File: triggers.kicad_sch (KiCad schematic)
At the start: 37 parts, among them U10 SN74LVC2G17DC, U13 SRV05-4, U14 SN74LVC2G17DC, U15 SRV05-4, U28 74HC14, U9 SN74LVC2G17DC

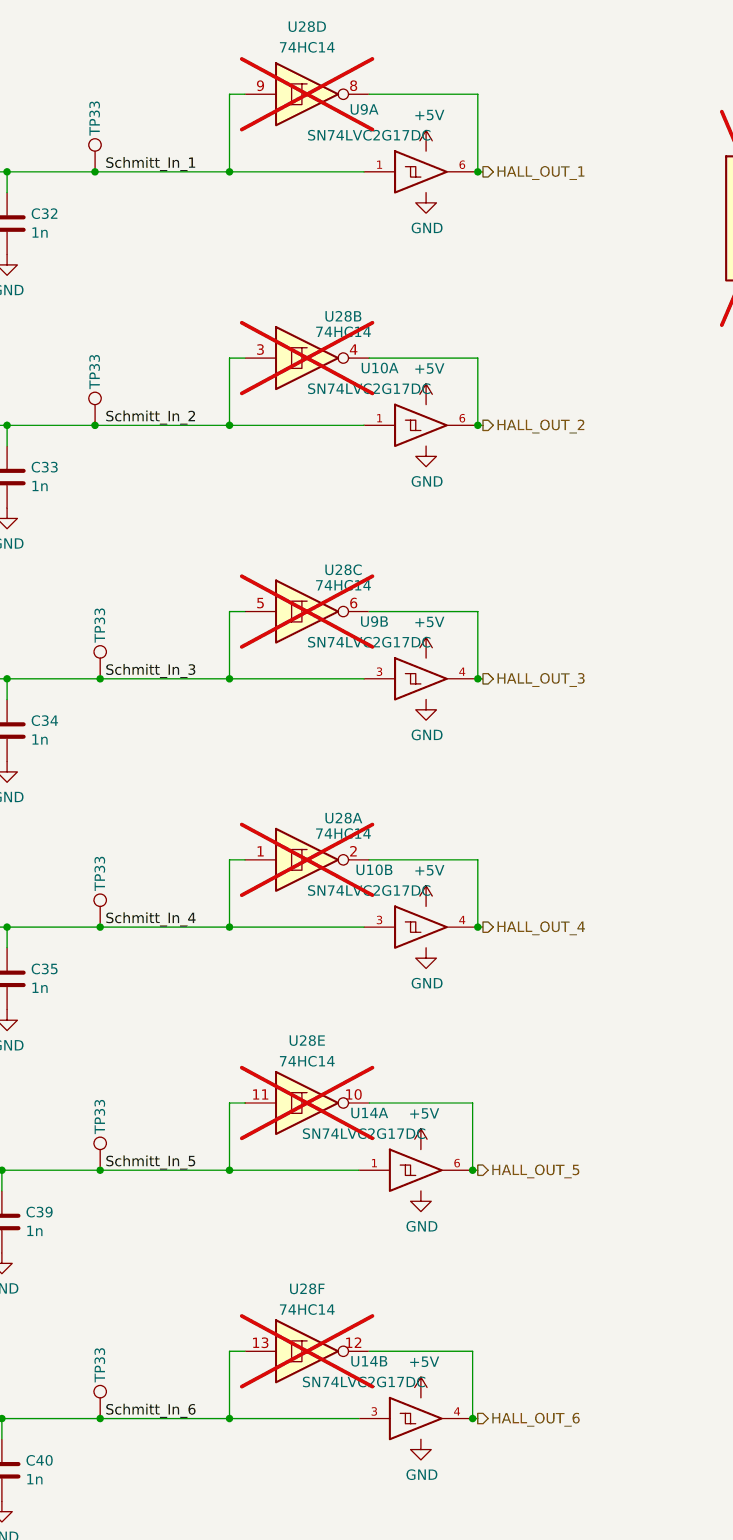
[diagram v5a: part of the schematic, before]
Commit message: Change U9,U10,U14 to SN74LVC2G17DBVR, version as ordered
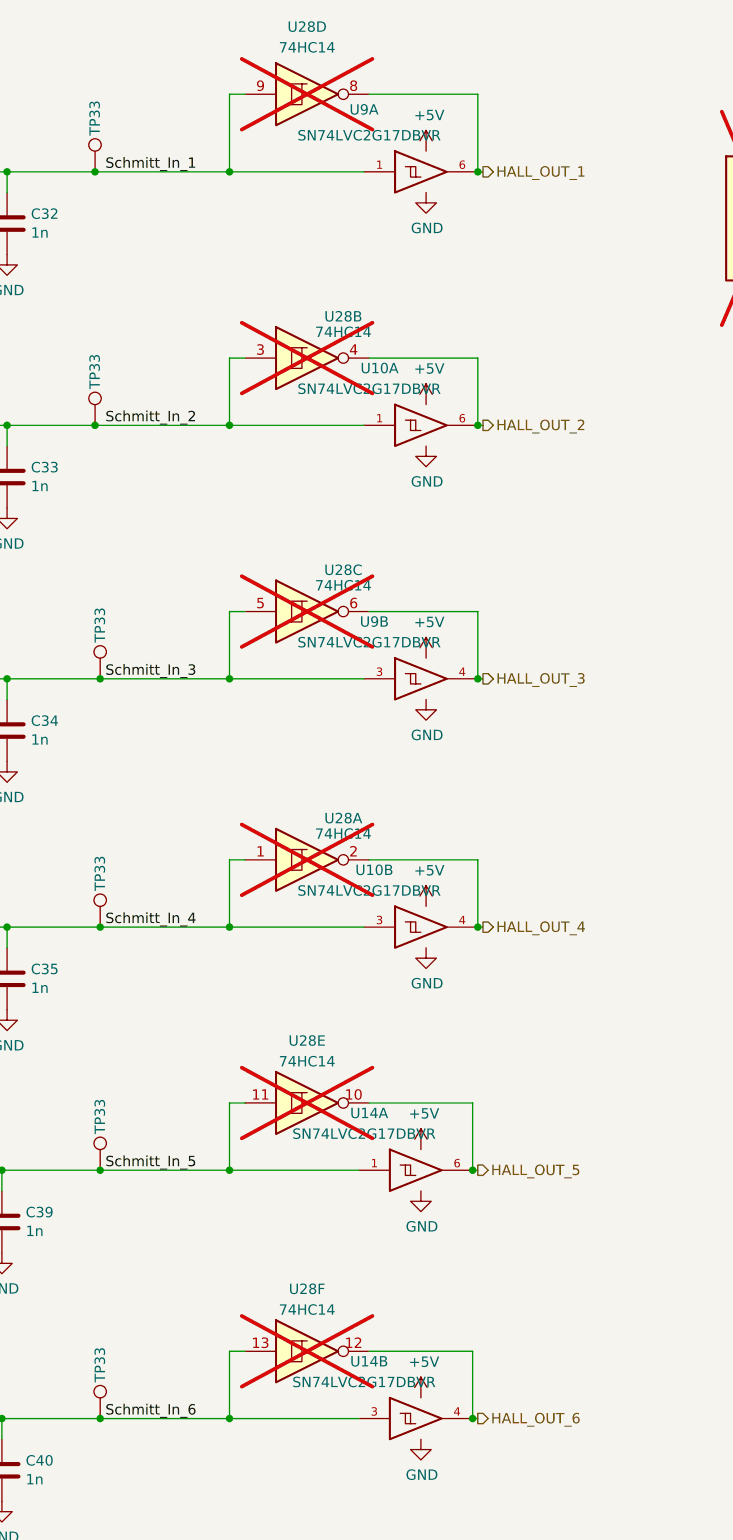
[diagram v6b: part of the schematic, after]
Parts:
- U10, U14, U9: value SN74LVC2G17DC -> SN74LVC2G17DBVR; footprint Package_TO_SOT_SMD:SOT-363_SC-70-6 -> Package_TO_SOT_SMD:SOT-23-6; JLCRotOffset (none) -> 90; LCSC C50714 -> C10429
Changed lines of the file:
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@@
       (effects (font (size 1.27 1.27)))
     )
-    (property "Value" "SN74LVC2G17DC" (at 94.615 85.725 0)
-      (effects (font (size 1.27 1.27)))
-    )
-    (property "Footprint" "Package_TO_SOT_SMD:SOT-363_SC-70-6" (at 101.6 90.17 0)
+    (property "Value" "SN74LVC2G17DBVR" (at 94.615 85.725 0)
+      (effects (font (size 1.27 1.27)))
+    )
+    (property "Footprint" "Package_TO_SOT_SMD:SOT-23-6" (at 101.6 90.17 0)
       (effects (font (size 1.27 1.27)) hide)
     )
@@
       (effects (font (size 1.27 1.27)) hide)
     )
-    (property "LCSC" "C50714" (at 101.6 90.17 0)
+    (property "LCSC" "C10429" (at 101.6 90.17 0)
       (effects (font (size 1.27 1.27)) hide)
     )
     (property "LCSC_ext" "1" (at 101.6 90.17 0)
+      (effects (font (size 1.27 1.27)) hide)
+    )
+    (property "JLCRotOffset" "90" (at 101.6 90.17 0)
       (effects (font (size 1.27 1.27)) hide)
     )
@@
       (effects (font (size 1.27 1.27)))
     )
-    (property "Value" "SN74LVC2G17DC" (at 94.615 54.61 0)
-      (effects (font (size 1.27 1.27)))
-    )
-    (property "Footprint" "Package_TO_SOT_SMD:SOT-363_SC-70-6" (at 101.6 59.055 0)
+    (property "Value" "SN74LVC2G17DBVR" (at 94.615 54.61 0)
+      (effects (font (size 1.27 1.27)))
+    )
+    (property "Footprint" "Package_TO_SOT_SMD:SOT-23-6" (at 101.6 59.055 0)
       (effects (font (size 1.27 1.27)) hide)
     )
@@
       (effects (font (size 1.27 1.27)) hide)
     )
-    (property "LCSC" "C50714" (at 101.6 59.055 0)
+    (property "LCSC" "C10429" (at 101.6 59.055 0)
       (effects (font (size 1.27 1.27)) hide)
     )
     (property "LCSC_ext" "1" (at 101.6 59.055 0)
+      (effects (font (size 1.27 1.27)) hide)
+    )
+    (property "JLCRotOffset" "90" (at 101.6 59.055 0)
       (effects (font (size 1.27 1.27)) hide)
     )
@@
       (effects (font (size 1.27 1.27)))
     )
-    (property "Value" "SN74LVC2G17DC" (at 94.615 23.495 0)
-      (effects (font (size 1.27 1.27)))
-    )
-    (property "Footprint" "Package_TO_SOT_SMD:SOT-363_SC-70-6" (at 101.6 27.94 0)
+    (property "Value" "SN74LVC2G17DBVR" (at 94.615 23.495 0)
+      (effects (font (size 1.27 1.27)))
+    )
+    (property "Footprint" "Package_TO_SOT_SMD:SOT-23-6" (at 101.6 27.94 0)
       (effects (font (size 1.27 1.27)) hide)
     )
@@
       (effects (font (size 1.27 1.27)) hide)
     )
-    (property "LCSC" "C50714" (at 101.6 27.94 0)
+    (property "LCSC" "C10429" (at 101.6 27.94 0)
       (effects (font (size 1.27 1.27)) hide)
     )
     (property "LCSC_ext" "1" (at 101.6 27.94 0)
+      (effects (font (size 1.27 1.27)) hide)
+    )
+    (property "JLCRotOffset" "90" (at 101.6 27.94 0)
       (effects (font (size 1.27 1.27)) hide)
     )
@@
       (effects (font (size 1.27 1.27)))
     )
-    (property "Value" "SN74LVC2G17DC" (at 93.98 176.53 0)
-      (effects (font (size 1.27 1.27)))
-    )
-    (property "Footprint" "Package_TO_SOT_SMD:SOT-363_SC-70-6" (at 100.965 180.975 0)
+    (property "Value" "SN74LVC2G17DBVR" (at 93.98 176.53 0)
+      (effects (font (size 1.27 1.27)))
+    )
+    (property "Footprint" "Package_TO_SOT_SMD:SOT-23-6" (at 100.965 180.975 0)
       (effects (font (size 1.27 1.27)) hide)
     )
@@
       (effects (font (size 1.27 1.27)) hide)
     )
-    (property "LCSC" "C50714" (at 100.965 180.975 0)
+    (property "LCSC" "C10429" (at 100.965 180.975 0)
       (effects (font (size 1.27 1.27)) hide)
     )
     (property "LCSC_ext" "1" (at 100.965 180.975 0)
+      (effects (font (size 1.27 1.27)) hide)
+    )
+    (property "JLCRotOffset" "90" (at 100.965 180.975 0)
       (effects (font (size 1.27 1.27)) hide)
     )
@@
       (effects (font (size 1.27 1.27)))
     )
-    (property "Value" "SN74LVC2G17DC" (at 93.98 146.05 0)
-      (effects (font (size 1.27 1.27)))
-    )
-    (property "Footprint" "Package_TO_SOT_SMD:SOT-363_SC-70-6" (at 100.965 150.495 0)
+    (property "Value" "SN74LVC2G17DBVR" (at 93.98 146.05 0)
+      (effects (font (size 1.27 1.27)))
+    )
+    (property "Footprint" "Package_TO_SOT_SMD:SOT-23-6" (at 100.965 150.495 0)
       (effects (font (size 1.27 1.27)) hide)
     )
@@
       (effects (font (size 1.27 1.27)) hide)
     )
-    (property "LCSC" "C50714" (at 100.965 150.495 0)
+    (property "LCSC" "C10429" (at 100.965 150.495 0)
       (effects (font (size 1.27 1.27)) hide)
     )
     (property "LCSC_ext" "1" (at 100.965 150.495 0)
+      (effects (font (size 1.27 1.27)) hide)
+    )
+    (property "JLCRotOffset" "90" (at 100.965 150.495 0)
       (effects (font (size 1.27 1.27)) hide)
     )
@@
       (effects (font (size 1.27 1.27)))
     )
-    (property "Value" "SN74LVC2G17DC" (at 94.615 116.205 0)
-      (effects (font (size 1.27 1.27)))
-    )
-    (property "Footprint" "Package_TO_SOT_SMD:SOT-363_SC-70-6" (at 101.6 120.65 0)
+    (property "Value" "SN74LVC2G17DBVR" (at 94.615 116.205 0)
+      (effects (font (size 1.27 1.27)))
+    )
+    (property "Footprint" "Package_TO_SOT_SMD:SOT-23-6" (at 101.6 120.65 0)
       (effects (font (size 1.27 1.27)) hide)
     )
@@
       (effects (font (size 1.27 1.27)) hide)
     )
-    (property "LCSC" "C50714" (at 101.6 120.65 0)
+    (property "LCSC" "C10429" (at 101.6 120.65 0)
       (effects (font (size 1.27 1.27)) hide)
     )
@@
       (effects (font (size 1.27 1.27)) hide)
     )
+    (property "JLCRotOffset" "90" (at 101.6 120.65 0)
+      (effects (font (size 1.27 1.27)) hide)
+    )
